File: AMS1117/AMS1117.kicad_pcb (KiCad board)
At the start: 2 copper layers, 9.9 x 12.4 mm, 4 parts, among them P1 CONN_01X03, U1 AMS1117-3.3

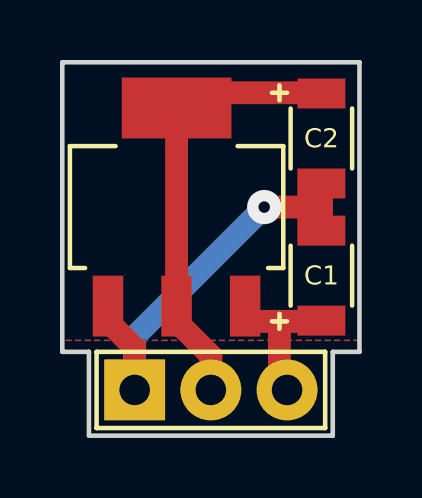
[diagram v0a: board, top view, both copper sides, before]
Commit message: AMS1117: Pass the redundant Vout through the via.
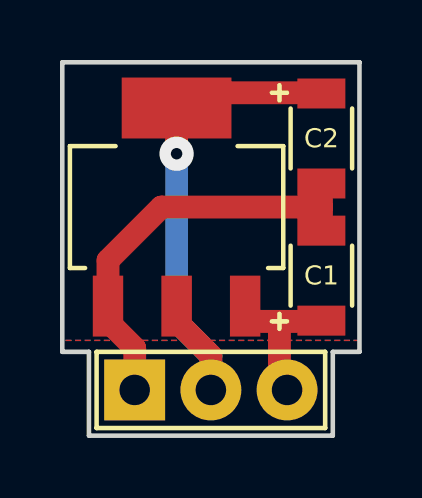
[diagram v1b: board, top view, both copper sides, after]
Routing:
- net VCC: track 15.5 -> 18.2 mm, vias 0 -> 1
- net GND: track 14.5 -> 14.1 mm, vias 1 -> 0
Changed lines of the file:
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@@
     (thickness 1.6)
     (drawings 20)
-    (tracks 17)
+    (tracks 19)
     (zones 0)
     (modules 4)
@@
   (title_block
     (title "AMS1117 Breakout")
-    (date 2016-05-31)
-    (rev 1)
+    (date 2016-06-27)
+    (rev 2)
   )
   (layers
@@
     (effects (font (size 1.016 1.016) (thickness 0.2032)) (justify left mirror))
   )
-  (segment (start 43.942 43.815) (end 48.26 39.497) (width 0.762) (layer B.Cu) (net 1))
-  (segment (start 50.165 39.497) (end 48.26 39.497) (width 0.762) (layer F.Cu) (net 1))
-  (via (at 48.26 39.497) (size 1.143) (drill 0.381) (layers F.Cu B.Cu) (net 1))
-  (segment (start 43.942 43.815) (end 43.942 45.593) (width 0.762) (layer B.Cu) (net 1))
+  (segment (start 43.053 41.275) (end 44.831 39.497) (width 0.762) (layer F.Cu) (net 1))
+  (segment (start 43.053 43.307) (end 43.053 41.275) (width 0.762) (layer F.Cu) (net 1) (status 30))
+  (segment (start 50.165 39.497) (end 44.831 39.497) (width 0.762) (layer F.Cu) (net 1))
   (segment (start 50.165 38.735) (end 50.165 39.497) (width 0.762) (layer F.Cu) (net 1))
   (segment (start 50.165 39.497) (end 50.165 40.259) (width 0.762) (layer F.Cu) (net 1))
   (segment (start 43.942 45.593) (end 43.942 44.196) (width 0.762) (layer F.Cu) (net 1))
   (segment (start 43.942 44.196) (end 43.053 43.307) (width 0.762) (layer F.Cu) (net 1) (status 20))
-  (segment (start 43.053 43.307) (end 43.053 42.799) (width 0.762) (layer F.Cu) (net 1) (status 30))
+  (segment (start 45.339 35.687) (end 45.339 37.719) (width 0.762) (layer F.Cu) (net 2))
+  (via (at 45.339 37.719) (size 1.143) (drill 0.381) (layers F.Cu B.Cu) (net 2))
+  (segment (start 45.339 37.719) (end 45.339 43.307) (width 0.762) (layer B.Cu) (net 2))
+  (segment (start 45.339 43.307) (end 46.482 44.45) (width 0.762) (layer B.Cu) (net 2))
+  (segment (start 46.482 44.45) (end 46.482 45.593) (width 0.762) (layer B.Cu) (net 2))
   (segment (start 50.419 35.687) (end 45.339 35.687) (width 0.762) (layer F.Cu) (net 2) (status 20))
-  (segment (start 45.339 35.687) (end 45.339 43.307) (width 0.762) (layer F.Cu) (net 2) (status 30))
   (segment (start 45.339 43.307) (end 46.482 44.45) (width 0.762) (layer F.Cu) (net 2) (status 10))
   (segment (start 46.482 44.45) (end 46.482 45.593) (width 0.762) (layer F.Cu) (net 2))
